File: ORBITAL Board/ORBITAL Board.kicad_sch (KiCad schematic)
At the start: 92 parts, among them J1 Conn_01x02, J2 Micro_SD_Card_Det, J3 Conn_01x12, J4 Conn_01x12, P1 USB_C_Plug_USB2.0, SW1 SW_DPST_x2, U1 PTPS563206DRLR, U2 W25Q128JVS, U3 USBLC6-2SC6, U4 LTC3118, U5 RP2040, U6 STSPIN220, U8 MS5607-02BA, Y1 ABLS-12.000MHZ-B4-T

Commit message: Updating SD Card to enable SPI comms. with RP2040
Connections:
- net +3.3V: now also U6.13 (EN/FLT), U6.14 (STBY/RESET)
- net D2: now also U6.16 (MODE1)
- net D3: now also U6.15 (MODE2)
- net D6: no longer C25.1, R18.1, U6.13 (EN/FLT)
- net D7: no longer C27.1, R19.1, U6.14 (STBY/RESET)
- net CLK_OUT: no longer names the net of U5.35 (GPIO23)
- net CLK_OUT: no longer J2.5 (CLK)
- net SD_CMD: no longer names the net of U5.18 (GPIO15)
- net SD_CMD: no longer J2.3 (CMD)
- net SD_DAT0 renamed SD_DOUT
- net SD_DAT1: no longer names the net of J2.8 (DAT1)
- net SD_DAT1: no longer U5.28 (GPIO17)
- net SD_DAT2: no longer names the net of J2.1 (DAT2)
- net SD_DAT2: no longer U5.29 (GPIO18)
- net SD_DAT3 renamed SD_CS
- net SD_CS: now also U5.28 (GPIO17); no longer U5.30 (GPIO19)
- new net: C25.1, R18.1
- new net: C27.1, R19.1
- new net SD_DIN: J2.3 (CMD), U5.30 (GPIO19)
- new net SD_SCLK: J2.5 (CLK), U5.29 (GPIO18)
- no-connect marks 5 -> 7
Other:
- note added: "SD Card is set for SPI interfacing with RP2040"
- note removed: "SD Card check Buck boost efficeny"
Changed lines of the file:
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@@
   (junction (at 215.9 109.22) (diameter 0) (color 0 0 0 0)
   )
-  (junction (at 228.6 40.64) (diameter 0) (color 0 0 0 0)
-  )
   (junction (at 153.67 64.77) (diameter 0) (color 0 0 0 0)
   )
@@
   (junction (at 271.78 151.13) (diameter 0) (color 0 0 0 0)
   )
+  (junction (at 251.46 40.64) (diameter 0) (color 0 0 0 0)
+  )
   (junction (at 120.65 39.37) (diameter 0) (color 0 0 0 0)
   )
@@
   (junction (at 378.46 162.56) (diameter 0) (color 0 0 0 0)
   )
-  (junction (at 236.22 43.18) (diameter 0) (color 0 0 0 0)
-  )
   (junction (at 248.158 65.786) (diameter 0) (color 0 0 0 0)
   )
@@
   (junction (at 189.23 101.6) (diameter 0) (color 0 0 0 0)
   )
+  (no_connect (at 66.04 190.5))
   (no_connect (at 368.3 149.86))
   (no_connect (at 44.45 49.53))
   (no_connect (at 66.04 213.36))
+  (no_connect (at 66.04 208.28))
   (no_connect (at 66.04 210.82))
   (no_connect (at 44.45 52.07))
@@
     (stroke (width 0) (type default))
   )
-  (wire (pts (xy 251.46 43.18) (xy 236.22 43.18))
-    (stroke (width 0) (type default))
-  )
   (wire (pts (xy 129.54 110.49) (xy 129.54 118.11))
     (stroke (width 0) (type default))
@@
     (stroke (width 0) (type default))
   )
-  (wire (pts (xy 228.6 40.64) (xy 228.6 40.386))
-    (stroke (width 0) (type default))
-  )
   (polyline (pts (xy 58.42 83.82) (xy 58.42 118.11))
     (stroke (width 0) (type default))
@@
     (stroke (width 0) (type default))
   )
-  (wire (pts (xy 251.46 40.64) (xy 228.6 40.64))
-    (stroke (width 0) (type default))
-  )
   (polyline (pts (xy 341.63 127) (xy 341.63 171.45))
     (stroke (width 0) (type default))
@@
     (stroke (width 0) (type default))
   )
-  (wire (pts (xy 228.6 41.91) (xy 228.6 40.64))
+  (wire (pts (xy 228.6 40.386) (xy 228.6 41.91))
     (stroke (width 0) (type default))
   )
@@
     (stroke (width 0) (type default))
   )
+  (wire (pts (xy 251.46 40.64) (xy 251.46 43.18))
+    (stroke (width 0) (type default))
+  )
   (wire (pts (xy 134.62 41.91) (xy 127 41.91))
     (stroke (width 0) (type default))
@@
     (effects (font (size 1.27 1.27) (thickness 0.254) bold) (justify left bottom))
   )
-  (text "SD Card check\nBuck boost efficeny" (at 118.11 231.14 0)
-    (effects (font (size 3 3) bold) (justify left bottom))
+  (text "SD Card is set for SPI interfacing with RP2040\n" (at 21.59 228.6 0)
+    (effects (font (size 1.5 1.5) bold) (justify left bottom))
   )
   (text "SD Card" (at 76.2 231.14 0)
@@
     (effects (font (size 1.27 1.27)) (justify left))
   )
-  (hierarchical_label "SD_DAT1" (shape input) (at 66.04 208.28 0) (fields_autoplaced)
-    (effects (font (size 1.27 1.27)) (justify left))
-  )
   (hierarchical_label "D9" (shape input) (at 269.24 203.2 0) (fields_autoplaced)
     (effects (font (size 1.27 1.27)) (justify left))
@@
     (effects (font (size 1.27 1.27)) (justify left))
   )
-  (hierarchical_label "SD_DAT1" (shape input) (at 269.24 223.52 0) (fields_autoplaced)
+  (hierarchical_label "SD_CS" (shape input) (at 269.24 223.52 0) (fields_autoplaced)
     (effects (font (size 1.27 1.27)) (justify left))
   )
@@
     (effects (font (size 1.27 1.27)) (justify left))
   )
-  (hierarchical_label "CLK_OUT" (shape input) (at 269.24 238.76 0) (fields_autoplaced)
-    (effects (font (size 1.27 1.27)) (justify left))
-  )
   (hierarchical_label "QSPI_SD2" (shape input) (at 67.31 153.67 0) (fields_autoplaced)
     (effects (font (size 1.27 1.27)) (justify left))
@@
     (effects (font (size 1.27 1.27)) (justify right))
   )
-  (hierarchical_label "SD_CMD" (shape input) (at 269.24 218.44 0) (fields_autoplaced)
-    (effects (font (size 1.27 1.27)) (justify left))
-  )
   (hierarchical_label "D0" (shape input) (at 269.24 180.34 0) (fields_autoplaced)
     (effects (font (size 1.27 1.27)) (justify left))
@@
     (effects (font (size 1.27 1.27)) (justify right))
   )
+  (hierarchical_label "SD_SCLK" (shape input) (at 269.24 226.06 0) (fields_autoplaced)
+    (effects (font (size 1.27 1.27)) (justify left))
+  )
   (hierarchical_label "D5" (shape input) (at 364.49 218.44 180) (fields_autoplaced)
     (effects (font (size 1.27 1.27)) (justify right))
@@
     (effects (font (size 1.27 1.27)) (justify right))
   )
+  (hierarchical_label "SD_DOUT" (shape input) (at 269.24 220.98 0) (fields_autoplaced)
+    (effects (font (size 1.27 1.27)) (justify left))
+  )
   (hierarchical_label "D9" (shape input) (at 364.49 228.6 180) (fields_autoplaced)
     (effects (font (size 1.27 1.27)) (justify right))
@@
     (effects (font (size 1.27 1.27)) (justify right))
   )
-  (hierarchical_label "SD_CMD" (shape input) (at 66.04 195.58 0) (fields_autoplaced)
+  (hierarchical_label "SD_DIN" (shape input) (at 66.04 195.58 0) (fields_autoplaced)
     (effects (font (size 1.27 1.27)) (justify left))
   )
@@
     (effects (font (size 1.27 1.27)) (justify right))
   )
-  (hierarchical_label "SD_DAT0" (shape input) (at 66.04 205.74 0) (fields_autoplaced)
+  (hierarchical_label "SD_DOUT" (shape input) (at 66.04 205.74 0) (fields_autoplaced)
     (effects (font (size 1.27 1.27)) (justify left))
   )
@@
     (effects (font (size 1.27 1.27)) (justify left))
   )
-  (hierarchical_label "D2" (shape input) (at 251.206 33.02 180) (fields_autoplaced)
+  (hierarchical_label "D2" (shape input) (at 251.46 33.02 180) (fields_autoplaced)
     (effects (font (size 1.27 1.27)) (justify right))
   )
@@
     (effects (font (size 1.27 1.27)) (justify right))
   )
-  (hierarchical_label "D7" (shape input) (at 234.95 43.18 180) (fields_autoplaced)
-    (effects (font (size 1.27 1.27)) (justify right))
-  )
-  (hierarchical_label "SD_DAT2" (shape input) (at 269.24 226.06 0) (fields_autoplaced)
-    (effects (font (size 1.27 1.27)) (justify left))
-  )
   (hierarchical_label "D+" (shape input) (at 276.86 170.18 0) (fields_autoplaced)
     (effects (font (size 1.27 1.27)) (justify left))
@@
     (effects (font (size 1.27 1.27)) (justify right))
   )
-  (hierarchical_label "SD_DAT3" (shape input) (at 269.24 228.6 0) (fields_autoplaced)
-    (effects (font (size 1.27 1.27)) (justify left))
-  )
   (hierarchical_label "D5" (shape input) (at 269.24 193.04 0) (fields_autoplaced)
     (effects (font (size 1.27 1.27)) (justify left))
   )
-  (hierarchical_label "SD_DAT3" (shape input) (at 66.04 193.04 0) (fields_autoplaced)
-    (effects (font (size 1.27 1.27)) (justify left))
-  )
-  (hierarchical_label "SD_DAT0" (shape input) (at 269.24 220.98 0) (fields_autoplaced)
+  (hierarchical_label "SD_CS" (shape input) (at 66.04 193.04 0) (fields_autoplaced)
     (effects (font (size 1.27 1.27)) (justify left))
   )
@@
     (effects (font (size 1.27 1.27)) (justify left))
   )
-  (hierarchical_label "SD_DAT2" (shape input) (at 66.04 190.5 0) (fields_autoplaced)
+  (hierarchical_label "SD_DIN" (shape input) (at 269.24 228.6 0) (fields_autoplaced)
     (effects (font (size 1.27 1.27)) (justify left))
   )
-  (hierarchical_label "D3" (shape input) (at 251.206 35.56 180) (fields_autoplaced)
+  (hierarchical_label "D3" (shape input) (at 251.46 35.56 180) (fields_autoplaced)
     (effects (font (size 1.27 1.27)) (justify right))
   )
@@
     (effects (font (size 1.27 1.27)) (justify left))
   )
-  (hierarchical_label "CLK_OUT" (shape input) (at 66.04 200.66 0) (fields_autoplaced)
+  (hierarchical_label "SD_SCLK" (shape input) (at 66.04 200.66 0) (fields_autoplaced)
     (effects (font (size 1.27 1.27)) (justify left))
   )
@@
     (effects (font (size 1.27 1.27)) (justify right))
   )
-  (hierarchical_label "D6" (shape input) (at 228.6 40.64 180) (fields_autoplaced)
-    (effects (font (size 1.27 1.27)) (justify right))
-  )
   (hierarchical_label "D2" (shape input) (at 269.24 185.42 0) (fields_autoplaced)
     (effects (font (size 1.27 1.27)) (justify left))
@@
         )
       )
+    )
+  )
+  (symbol (lib_id "power:+3.3V") (at 251.46 40.64 90) (unit 1)
+    (in_bom yes) (on_board yes) (dnp no)
+    (property "Reference" "#PWR025" (at 255.27 40.64 0)
+      (effects (font (size 1.27 1.27)) hide)
+    )
+    (property "Value" "+3.3V" (at 247.65 39.37 0)
+      (effects (font (size 1.27 1.27)) (justify right))
+    )
+    (property "Footprint" "" (at 251.46 40.64 0)
+      (effects (font (size 1.27 1.27)) hide)
+    )
+    (property "Datasheet" "" (at 251.46 40.64 0)
+      (effects (font (size 1.27 1.27)) hide)
+    )
+    (pin "1")
+    (instances
+      (project "ORBITAL Board"
+        (path "/ed00f797-6c76-4d28-b3bc-c732d14de183"
+          (reference "#PWR025") (unit 1)
+        )
+      )

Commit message: Creating .2V Vref source for motor controller
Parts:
- added R29: 9000, Resistor_SMD:R_0603_1608Metric, symbol Device:R_Small
- added R30: 2000, Resistor_SMD:R_0603_1608Metric, symbol Device:R_Small
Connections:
- net +1V1: now also R29.2
- net +3.3V: no longer U6.13 (EN/FLT), U6.14 (STBY/RESET)
- net A3: no longer U6.11 (REF)
- net GND: now also R30.1
- net at C25.1, R18.1: now also U6.13 (EN/FLT)
- net at C27.1, R19.1: now also U6.14 (STBY/RESET)
- new net VRef: R29.1, R30.2, U6.11 (REF)
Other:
- note added: "Via Voltage Divider, VRef = .2V"
- moved on the sheet: C25

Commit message: Updating PCB Layout
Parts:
- J2: SPI Hookup (none) -> https://www.google.com/search?q=microsd+card+spi+pinout&rlz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
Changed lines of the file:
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@@
+      (effects (font (size 1.27 1.27)) hide)
+    )
+    (property "SPI Hookup" "https://www.google.com/search?q=microsd+card+spi+pinout&rlz=1C1ONGR_enUS1071US1071&oq=microsd+card+spi&gs_lcrp=EgZjaHJvbWUqCAgCEAAYFhgeMgkIABBFGDkYgAQyBwgBEAAYgAQyCAgCEAAYFhgeMggIAxAAGBYYHjIICAQQABgWGB4yCAgFEAAYFhgeMg0IBhAAGIYDGIAEGIoFMg0IBxAAGIYDGIAEGIoFMg0ICBAAGIYDGIAEGIoF0gEINTE4M2oxajmoAgCwAgA&sourceid=chrome&ie=UTF-8#vhid=9TkNl1FubUnFiM&vssid=l" (at 43.18 200.66 0)
       (effects (font (size 1.27 1.27)) hide)
     )

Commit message: Updating ORBITAL PCB
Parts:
- BT1: footprint BackupBattery:BAT_MS920SE-FL27E -> GPS:BT1
- D1: footprint GPS:DIO_RB400DFH_ROM-M -> GPS:DFLS130L
- U5: footprint RP2040_minimal:RP2040-QFN-56 -> RP2040:RP2040-QFN-56
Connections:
- net D13: now also U5.16 (GPIO13)
- net D14: now also U5.17 (GPIO14)
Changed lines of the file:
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@@
     (effects (font (size 1.27 1.27)) (justify right))
   )
+  (hierarchical_label "D13" (shape input) (at 269.24 213.36 0) (fields_autoplaced)
+    (effects (font (size 1.27 1.27)) (justify left))
+  )
   (hierarchical_label "D0" (shape input) (at 269.24 180.34 0) (fields_autoplaced)
     (effects (font (size 1.27 1.27)) (justify left))
@@
     (effects (font (size 1.27 1.27)) (justify right))
   )
+  (hierarchical_label "D14" (shape input) (at 269.24 215.9 0) (fields_autoplaced)
+    (effects (font (size 1.27 1.27)) (justify left))
+  )
   (hierarchical_label "D6" (shape input) (at 269.24 195.58 0) (fields_autoplaced)
     (effects (font (size 1.27 1.27)) (justify left))
@@
       (effects (font (size 1.27 1.27)) (justify left))
     )
-    (property "Footprint" "RP2040_minimal:RP2040-QFN-56" (at 218.44 213.36 0)
+    (property "Footprint" "RP2040:RP2040-QFN-56" (at 218.44 213.36 0)
       (effects (font (size 1.27 1.27)) hide)
     )
@@
       (effects (font (size 1.27 1.27)) (justify left))
     )
-    (property "Footprint" "BackupBattery:BAT_MS920SE-FL27E" (at 22.86 107.696 90)
+    (property "Footprint" "GPS:BT1" (at 22.86 107.696 90)
       (effects (font (size 1.27 1.27)) hide)
     )
@@
       (effects (font (size 1.27 1.27)) (justify right))
     )
-    (property "Footprint" "GPS:DIO_RB400DFH_ROM-M" (at 22.86 93.98 90)
+    (property "Footprint" "GPS:DFLS130L" (at 22.86 93.98 90)
       (effects (font (size 1.27 1.27)) hide)
     )

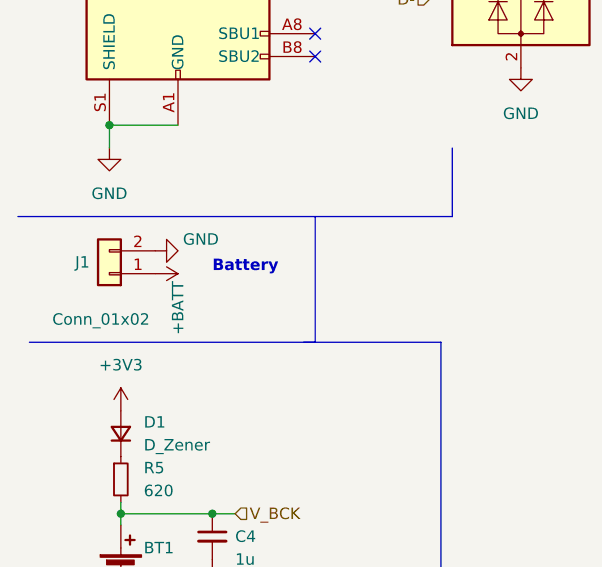
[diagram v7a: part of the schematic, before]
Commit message: Implementing Motor Controller into PCB
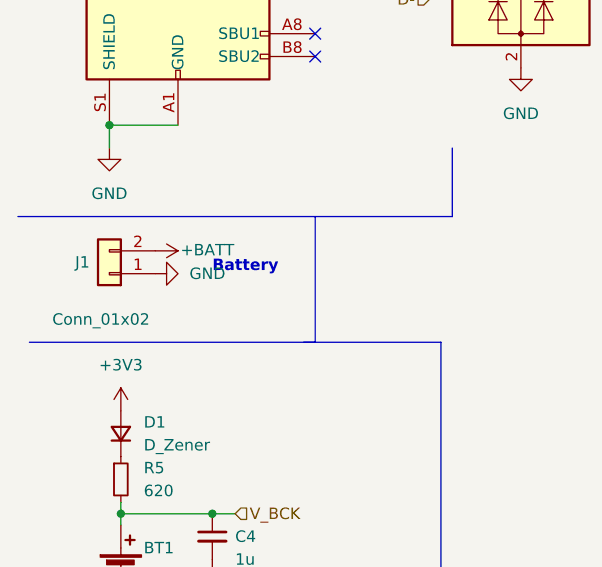
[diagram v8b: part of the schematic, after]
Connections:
- net +BATT: now also J1.2 (Pin_2); no longer J1.1 (Pin_1)
- net GND: now also J1.1 (Pin_1); no longer J1.2 (Pin_2)
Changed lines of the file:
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@@
-    )
-  )
-  (symbol (lib_id "power:GND") (at 26.67 73.66 90) (unit 1)
-    (in_bom yes) (on_board yes) (dnp no)
-    (property "Reference" "#PWR0126" (at 33.02 73.66 0)
-      (effects (font (size 1.27 1.27)) hide)
-    )
-    (property "Value" "GND" (at 31.75 72.39 90)
-      (effects (font (size 1.27 1.27)))
-    )
-    (property "Footprint" "" (at 26.67 73.66 0)
-      (effects (font (size 1.27 1.27)) hide)
-    )
-    (property "Datasheet" "" (at 26.67 73.66 0)
-      (effects (font (size 1.27 1.27)) hide)
-    )
-    (pin "1")
-    (instances
-      (project "ORBITAL Board"
-        (path "/ed00f797-6c76-4d28-b3bc-c732d14de183"
-          (reference "#PWR0126") (unit 1)
-        )
-      )
     )
   )
@@
     )
   )
+  (symbol (lib_id "power:+BATT") (at 26.67 73.66 270) (unit 1)
+    (in_bom yes) (on_board yes) (dnp no)
+    (property "Reference" "#PWR027" (at 22.86 73.66 0)
+      (effects (font (size 1.27 1.27)) hide)
+    )
+    (property "Value" "+BATT" (at 32.4687 73.5736 90)
+      (effects (font (size 1.27 1.27)))
+    )
+    (property "Footprint" "" (at 26.67 73.66 0)
+      (effects (font (size 1.27 1.27)) hide)
+    )
+    (property "Datasheet" "" (at 26.67 73.66 0)
+      (effects (font (size 1.27 1.27)) hide)
+    )
+    (pin "1")
+    (instances
+      (project "ORBITAL Board"
+        (path "/ed00f797-6c76-4d28-b3bc-c732d14de183"
+          (reference "#PWR027") (unit 1)
+        )
+      )
+    )
+  )
   (symbol (lib_id "Device:R_Small") (at 120.65 49.53 180) (unit 1)
     (in_bom yes) (on_board yes) (dnp no)
@@
     )
   )
-  (symbol (lib_id "power:+BATT") (at 26.67 76.2 270) (unit 1)
-    (in_bom yes) (on_board yes) (dnp no)
-    (property "Reference" "#PWR0125" (at 22.86 76.2 0)
-      (effects (font (size 1.27 1.27)) hide)
-    )
-    (property "Value" "+BATT" (at 29.21 80.01 0)
-      (effects (font (size 1.27 1.27)))
-    )
-    (property "Footprint" "" (at 26.67 76.2 0)
-      (effects (font (size 1.27 1.27)) hide)
-    )
-    (property "Datasheet" "" (at 26.67 76.2 0)
-      (effects (font (size 1.27 1.27)) hide)
-    )
-    (pin "1")
-    (instances
-      (project "ORBITAL Board"
-        (path "/ed00f797-6c76-4d28-b3bc-c732d14de183"
-          (reference "#PWR0125") (unit 1)
-        )
-      )
-    )
-  )
   (symbol (lib_id "power:GND") (at 351.79 27.94 180) (unit 1)
     (in_bom yes) (on_board yes) (dnp no) (fields_autoplaced)
@@
         )
       )
+    )
+  )
+  (symbol (lib_id "power:GND") (at 26.67 76.2 90) (unit 1)
+    (in_bom yes) (on_board yes) (dnp no) (fields_autoplaced)
+    (property "Reference" "#PWR028" (at 33.02 76.2 0)
+      (effects (font (size 1.27 1.27)) hide)
+    )
+    (property "Value" "GND" (at 30.48 76.2 90)
+      (effects (font (size 1.27 1.27)) (justify right))
+    )
+    (property "Footprint" "" (at 26.67 76.2 0)
+      (effects (font (size 1.27 1.27)) hide)
+    )
+    (property "Datasheet" "" (at 26.67 76.2 0)
+      (effects (font (size 1.27 1.27)) hide)
+    )
+    (pin "1")
+    (instances
+      (project "ORBITAL Board"
+        (path "/ed00f797-6c76-4d28-b3bc-c732d14de183"
+          (reference "#PWR028") (unit 1)
+        )
+      )
